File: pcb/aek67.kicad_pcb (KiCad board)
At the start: 2 copper layers, 304.8 x 100.4 mm, 154 parts, among them J1 AVR-ISP-6, K1 K_GRV, K10 K_9, K11 K_0, K12 K_MINUS, K13 K_EQUAL, K14 K_BACKSPACE, K15 K_PAGE_UP, K16 K_TAB, K17 K_Q, K18 K_W, K19 K_E, K2 K_1, K20 K_R, K21 K_T, K22 K_Y, K23 K_U, K24 K_I, K25 K_O, K26 K_P, K27 K_LBRC, K28 K_RBRC, K29 K_BSLSH, K3 K_2, K30 K_PAGE_DN, K31 K_CAPS_LOCK, K32 K_A, K33 K_S, K34 K_D, K35 K_F, K36 K_G, K37 K_H, K38 K_J, K39 K_K, K4 K_3, K40 K_L, K41 K_SEMIC, K42 K_QUOTE, K43 K_ENTER, K44 K_INSERT, K45 K_LSHIFT, K46 K_Z, K47 K_X, K48 K_C, K49 K_V, K5 K_4, K50 K_B, K51 K_N, K52 K_M, K53 K_COMMA, K54 K_DOT, K55 K_SLASH, K56 K_RSHIFT, K57 K_UP, K58 K_DELETE, K59 K_LCTRL, K6 K_5, K60 K_LAPP, K61 K_LALT, K62 K_SPC, K63 K_RALT, K64 K_RAPP, K65 K_LEFT, K66 K_DOWN, K67 K_RIGHT, K7 K_6, K8 K_7, K9 K_8, SW1 SW_PUSH, U1 ATmega32U4-AU, U2 PRTR5V0U2X, X1 XTAL_GND

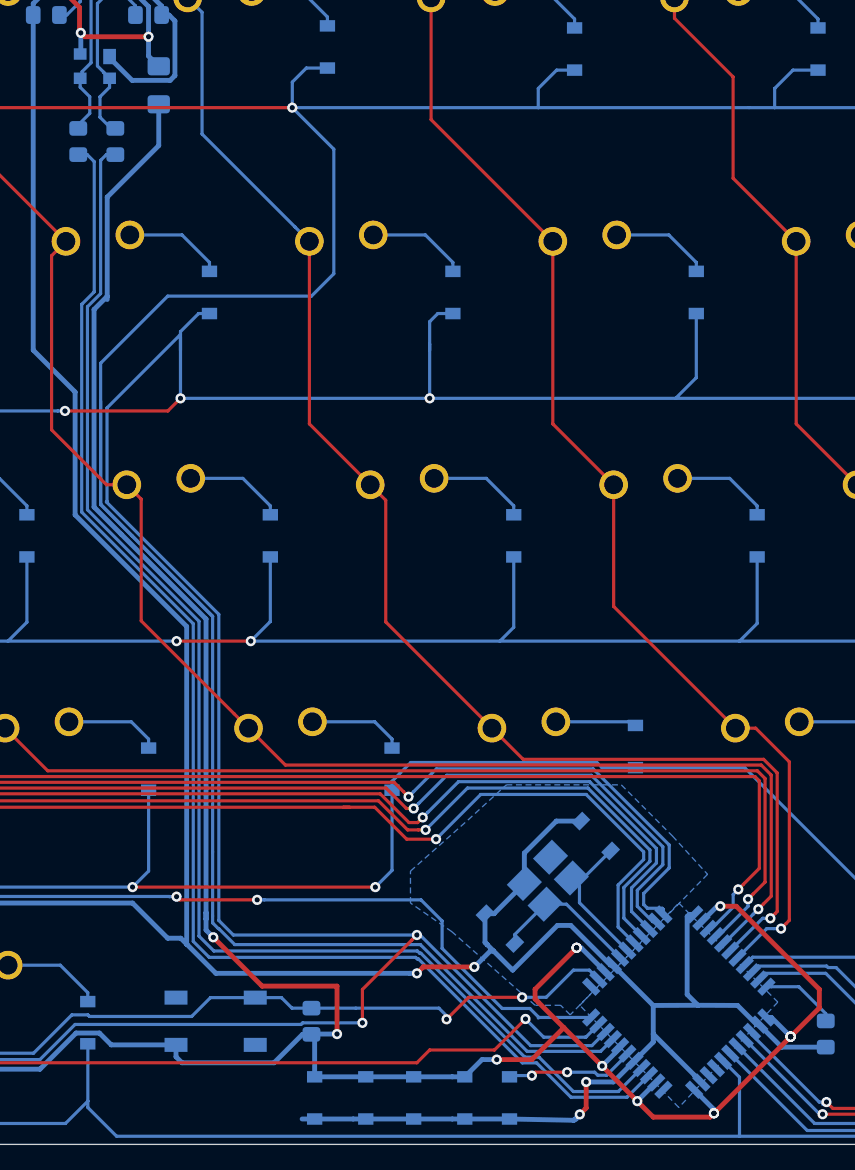
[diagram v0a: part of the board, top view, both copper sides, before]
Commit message: update capacitor footprints
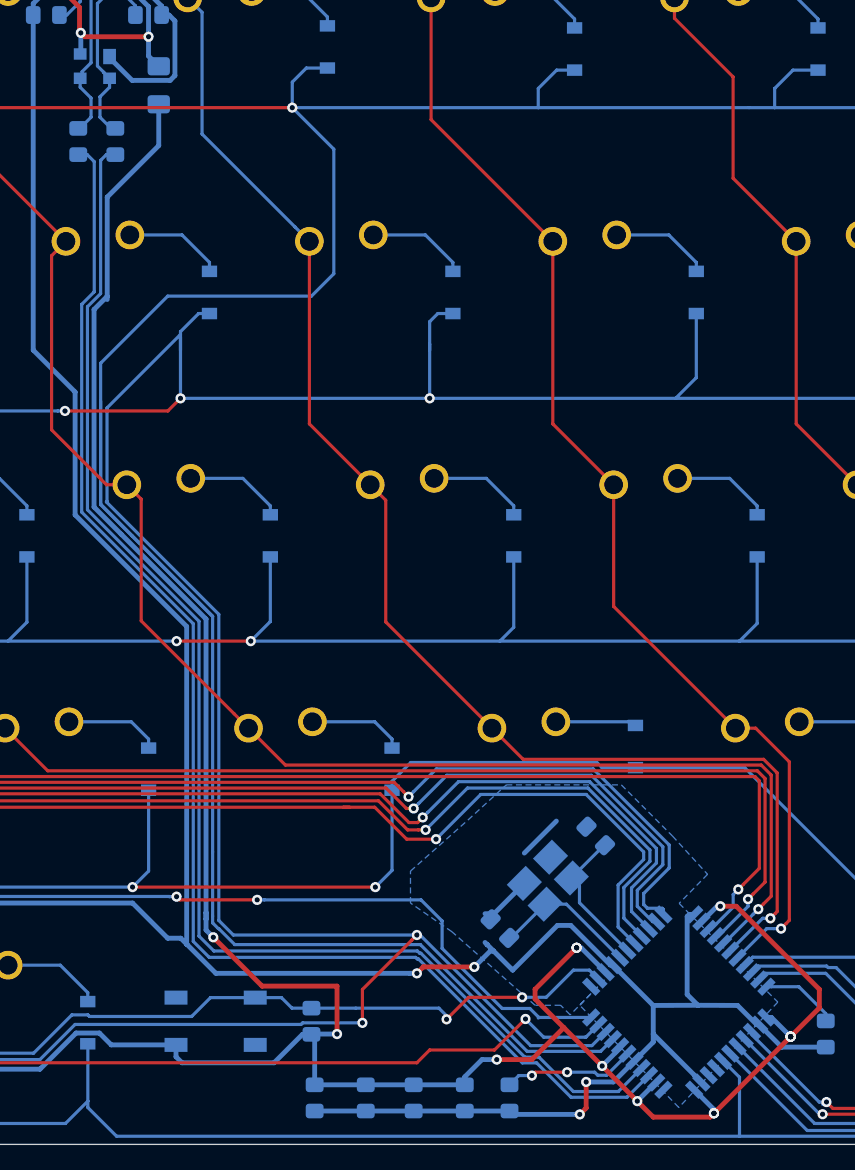
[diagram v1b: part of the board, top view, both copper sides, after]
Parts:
- C1, C2, C3, C4, C5, C6, C7: footprint Diode_SMD:D_SOD-123 -> Capacitor_SMD:C_0805_2012Metric_Pad1.15x1.40mm_HandSolder
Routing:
- net GND: track 294.5 -> 286.6 mm
- net +5V: track 236.9 -> 238.1 mm
- net XTAL1: track 11.5 -> 12.2 mm

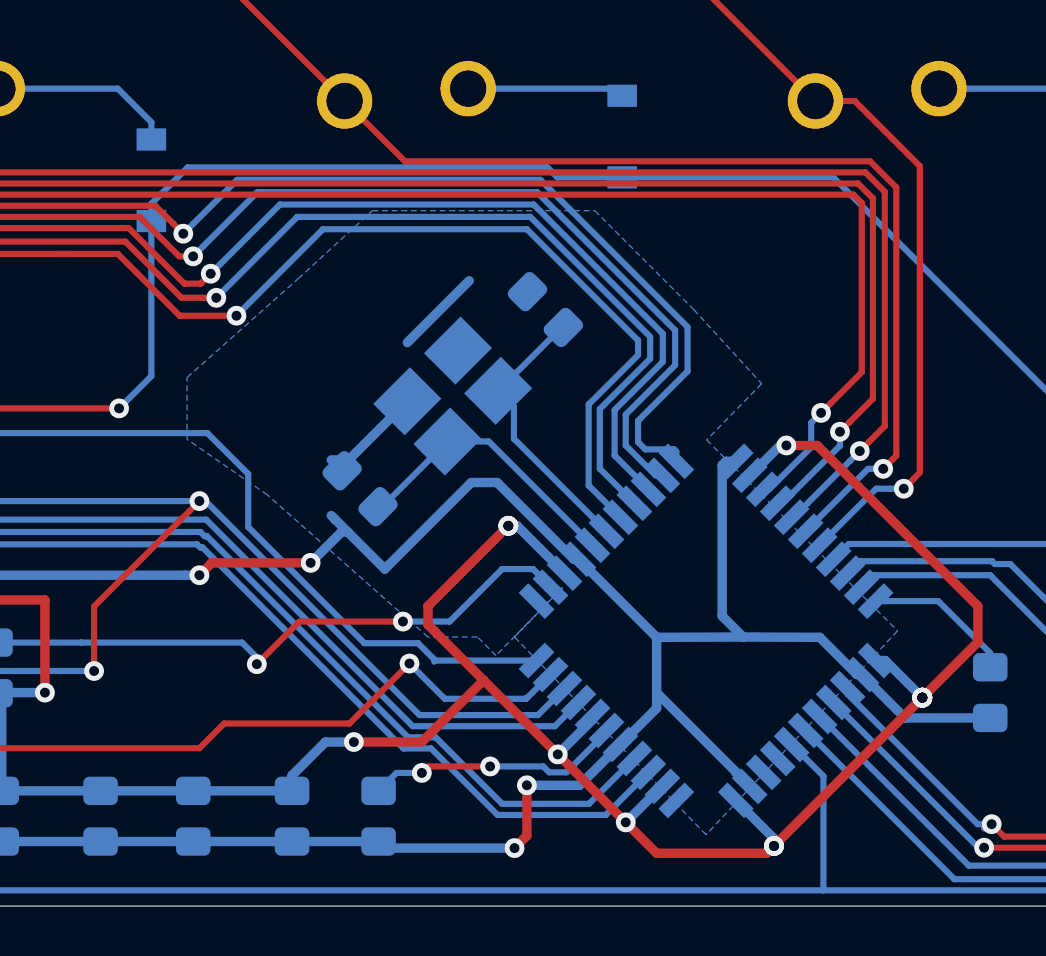
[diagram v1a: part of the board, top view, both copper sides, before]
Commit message: use the correct crystal footprints
with opposite XTAL pads, in consequence redid the GND zones
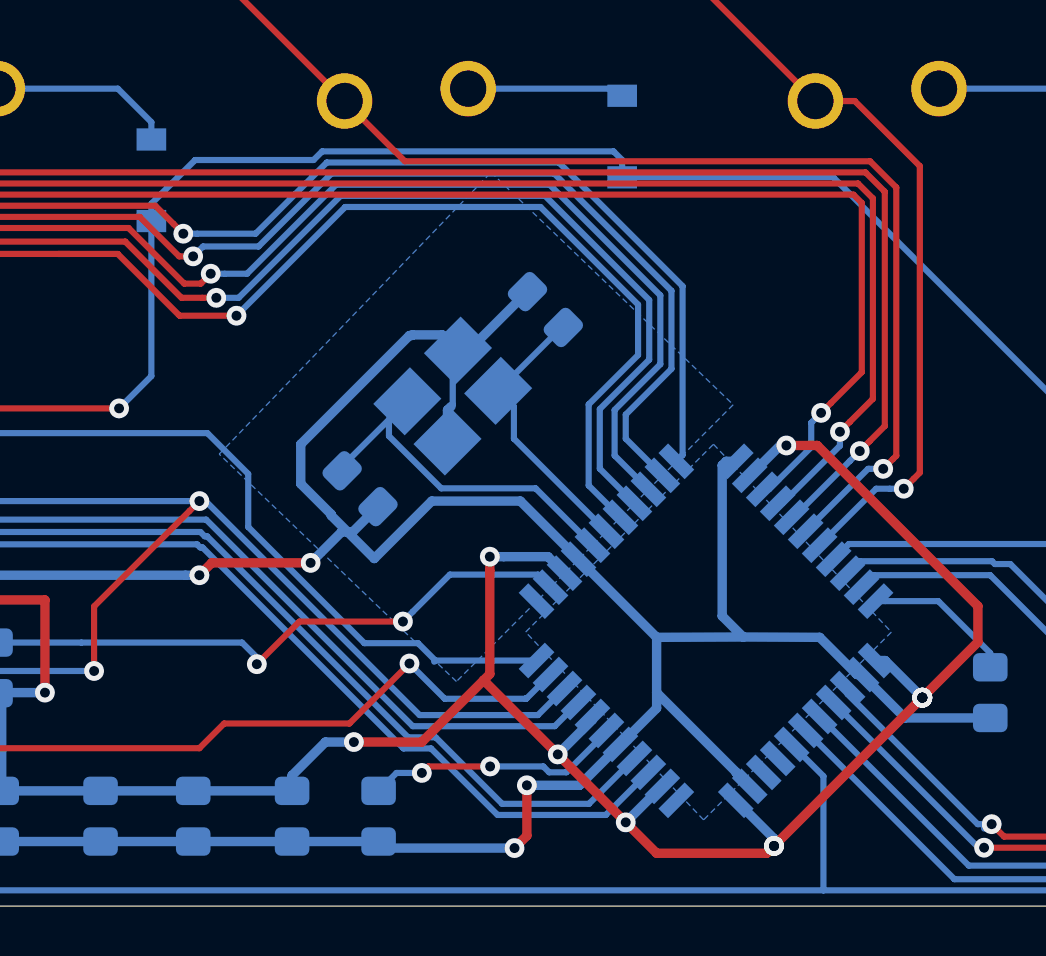
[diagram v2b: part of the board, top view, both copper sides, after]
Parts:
- turned C6 to 315 degrees
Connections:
- X1 pad 2: XTAL2 -> GND
- X1 pad 3: GND -> XTAL2
- X1 pad 4: (no net) -> GND
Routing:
- net GND: track 286.6 -> 299.0 mm
- net XTAL2: track 11.5 -> 15.7 mm
- net +5V: track 238.1 -> 234.9 mm, vias 14 -> 13
- net col0: track 277.4 -> 279.0 mm
- net col1: track 255.4 -> 256.9 mm
- net col2: track 230.0 -> 231.4 mm
- net col3: track 190.2 -> 191.4 mm
- net row3: track 413.0 -> 413.9 mm
- net col4: track 172.6 -> 171.9 mm

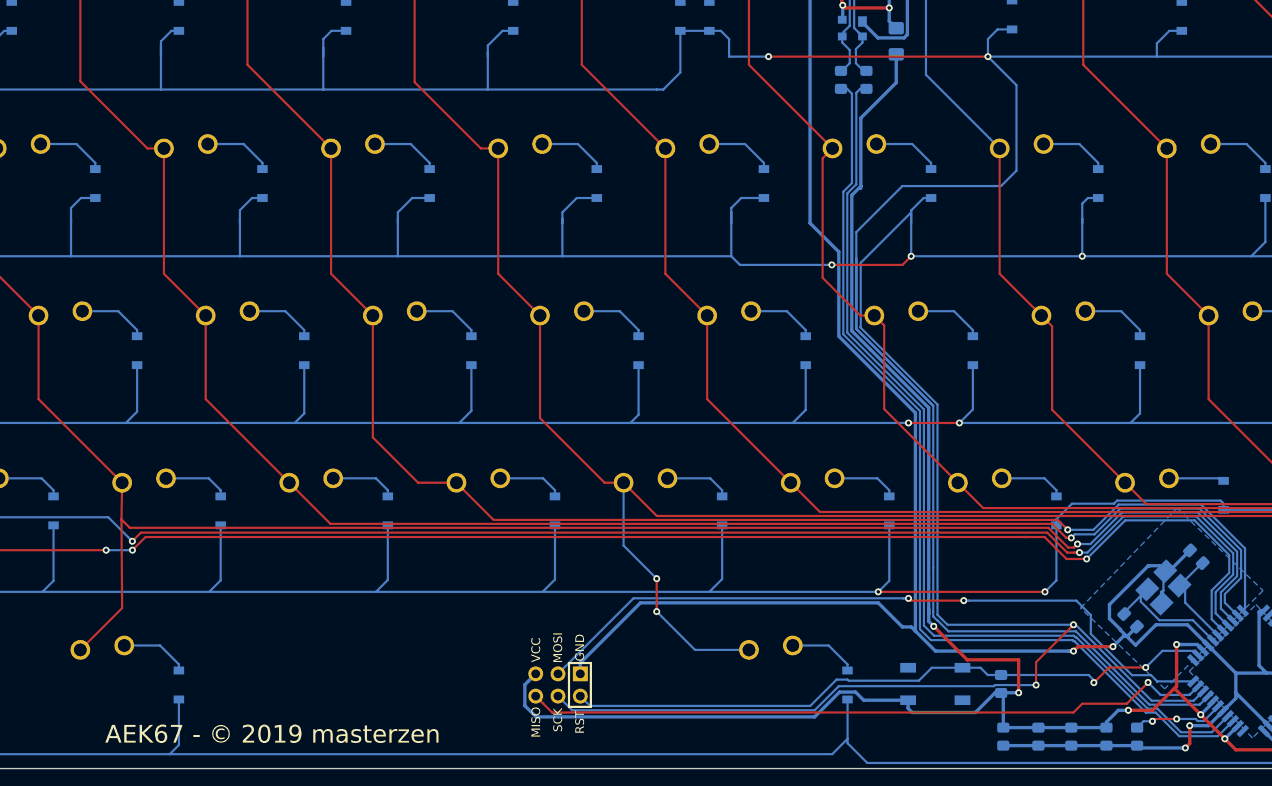
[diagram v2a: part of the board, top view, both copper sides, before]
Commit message: rerouted USB D+/D- signal for EMI protection
far from other signals
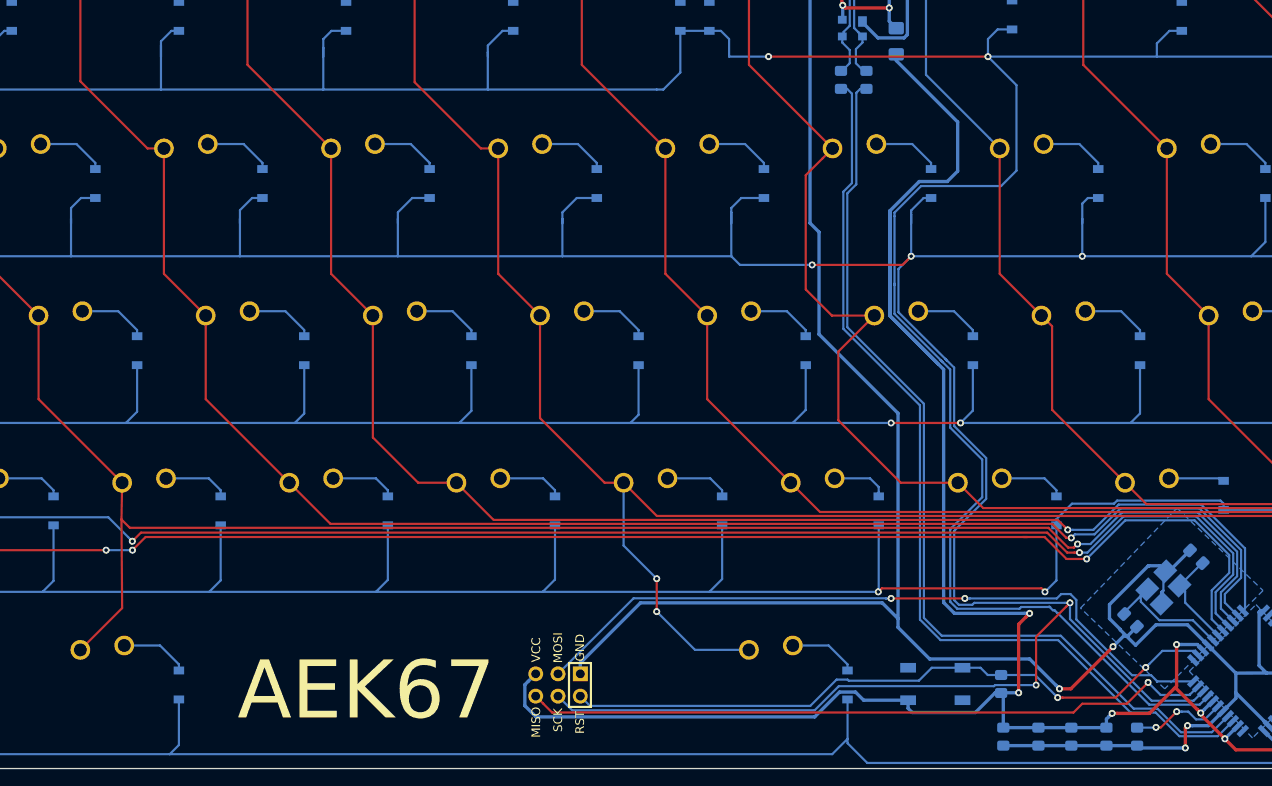
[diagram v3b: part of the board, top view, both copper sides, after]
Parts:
- moved D51 1.21 mm to (175.8, 86.5)
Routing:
- net +5V: track 234.9 -> 260.8 mm
- net row0: track 514.8 -> 491.2 mm
- net col7: track 126.1 -> 136.8 mm
- net SCLK: track 551.9 -> 548.1 mm
- net GND: track 299.0 -> 301.0 mm
- net RST: track 76.0 -> 77.3 mm
- net Net-(D51-Pad2): track 7.49 -> 6.32 mm
- net Net-(R3-Pad1): track 108.0 -> 107.3 mm
- net Net-(R2-Pad1): track 106.5 -> 106.0 mm
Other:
- board text added: "AEK67"
- board text added: "© 2019 masterzen"
- board text removed: "AEK67 - © 2019 masterzen"

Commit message: updated key text on front silks side
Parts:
- removed D1: D_GRV, Diode_SMD:D_SOD-123
- removed D10: D_9, Diode_SMD:D_SOD-123
- removed D11: D_0, Diode_SMD:D_SOD-123
- removed D12: D_MINUS, Diode_SMD:D_SOD-123
- removed D13: D_EQUAL, Diode_SMD:D_SOD-123
- removed D14: D_BACKSPACE, Diode_SMD:D_SOD-123
- removed D15: D_PAGE_UP, Diode_SMD:D_SOD-123
- removed D16: D_TAB, Diode_SMD:D_SOD-123
- removed D17: D_Q, Diode_SMD:D_SOD-123
- removed D18: D_W, Diode_SMD:D_SOD-123
- removed D19: D_E, Diode_SMD:D_SOD-123
- removed D2: D_1, Diode_SMD:D_SOD-123
- removed D20: D_R, Diode_SMD:D_SOD-123
- removed D21: D_T, Diode_SMD:D_SOD-123
- removed D22: D_Y, Diode_SMD:D_SOD-123
- removed D23: D_U, Diode_SMD:D_SOD-123
- removed D24: D_I, Diode_SMD:D_SOD-123
- removed D25: D_O, Diode_SMD:D_SOD-123
- removed D26: D_P, Diode_SMD:D_SOD-123
- removed D27: D_LBRC, Diode_SMD:D_SOD-123
- removed D28: D_RBRC, Diode_SMD:D_SOD-123
- removed D29: D_BSLSH, Diode_SMD:D_SOD-123
- removed D3: D_2, Diode_SMD:D_SOD-123
- removed D30: D_PAGE_DN, Diode_SMD:D_SOD-123
- removed D31: D_CAPS_LOCK, Diode_SMD:D_SOD-123
- removed D32: D_A, Diode_SMD:D_SOD-123
- removed D33: D_S, Diode_SMD:D_SOD-123
- removed D34: D_D, Diode_SMD:D_SOD-123
- removed D35: D_F, Diode_SMD:D_SOD-123
- removed D36: D_G, Diode_SMD:D_SOD-123
- removed D37: D_H, Diode_SMD:D_SOD-123
- removed D38: D_J, Diode_SMD:D_SOD-123
- removed D39: D_K, Diode_SMD:D_SOD-123
- removed D4: D_3, Diode_SMD:D_SOD-123
- removed D40: D_L, Diode_SMD:D_SOD-123
- removed D41: D_SEMIC, Diode_SMD:D_SOD-123
- removed D42: D_QUOTE, Diode_SMD:D_SOD-123
- removed D43: D_ENTER, Diode_SMD:D_SOD-123
- removed D44: D_INSERT, Diode_SMD:D_SOD-123
- removed D45: D_LSHIFT, Diode_SMD:D_SOD-123
- removed D46: D_Z, Diode_SMD:D_SOD-123
- removed D47: D_X, Diode_SMD:D_SOD-123
- removed D48: D_C, Diode_SMD:D_SOD-123
- removed D49: D_V, Diode_SMD:D_SOD-123
- removed D5: D_4, Diode_SMD:D_SOD-123
- removed D50: D_B, Diode_SMD:D_SOD-123
- removed D51: D_N, Diode_SMD:D_SOD-123
- removed D52: D_M, Diode_SMD:D_SOD-123
- removed D53: D_COMMA, Diode_SMD:D_SOD-123
- removed D54: D_DOT, Diode_SMD:D_SOD-123
- removed D55: D_SLASH, Diode_SMD:D_SOD-123
- removed D56: D_RSHIFT, Diode_SMD:D_SOD-123
- removed D57: D_UP, Diode_SMD:D_SOD-123
- removed D58: D_DELETE, Diode_SMD:D_SOD-123
- removed D59: D_LCTRL, Diode_SMD:D_SOD-123
- removed D6: D_5, Diode_SMD:D_SOD-123
- removed D60: D_LAPP, Diode_SMD:D_SOD-123
- removed D61: D_LALT, Diode_SMD:D_SOD-123
- removed D62: D_SPC, Diode_SMD:D_SOD-123
- removed D63: D_RALT, Diode_SMD:D_SOD-123
- removed D64: D_RAPP, Diode_SMD:D_SOD-123
- removed D65: D_LEFT, Diode_SMD:D_SOD-123
- removed D66: D_DOWN, Diode_SMD:D_SOD-123
- removed D67: D_RIGHT, Diode_SMD:D_SOD-123
- removed D7: D_6, Diode_SMD:D_SOD-123
- removed D8: D_7, Diode_SMD:D_SOD-123
- removed D9: D_8, Diode_SMD:D_SOD-123
- removed F1: 500, Fuse:Fuse_1206_3216Metric_Pad1.42x1.75mm_HandSolder
- removed J1: AVR-ISP-6, random-keyboard-parts:Reset_Pretty-Mask
- removed K1: K_GRV, Alps_Only:ALPS-1U
- removed K10: K_9, Alps_Only:ALPS-1U
- removed K11: K_0, Alps_Only:ALPS-1U
- removed K12: K_MINUS, Alps_Only:ALPS-1U
- removed K16: K_TAB, Alps_Only:ALPS-1.5U
- removed K17: K_Q, Alps_Only:ALPS-1U
- removed K18: K_W, Alps_Only:ALPS-1U
- removed K19: K_E, Alps_Only:ALPS-1U
- removed K2: K_1, Alps_Only:ALPS-1U
- removed K20: K_R, Alps_Only:ALPS-1U
- removed K21: K_T, Alps_Only:ALPS-1U
- removed K22: K_Y, Alps_Only:ALPS-1U
- removed K23: K_U, Alps_Only:ALPS-1U
- removed K24: K_I, Alps_Only:ALPS-1U
- removed K25: K_O, Alps_Only:ALPS-1U
- removed K26: K_P, Alps_Only:ALPS-1U
- removed K27: K_LBRC, Alps_Only:ALPS-1U
- removed K3: K_2, Alps_Only:ALPS-1U
- removed K31: K_CAPS_LOCK, Alps_Only:ALPS-1.75U
- removed K32: K_A, Alps_Only:ALPS-1U
- removed K33: K_S, Alps_Only:ALPS-1U
- removed K34: K_D, Alps_Only:ALPS-1U
- removed K35: K_F, Alps_Only:ALPS-1U
- removed K36: K_G, Alps_Only:ALPS-1U
- removed K37: K_H, Alps_Only:ALPS-1U
- removed K38: K_J, Alps_Only:ALPS-1U
- removed K39: K_K, Alps_Only:ALPS-1U
- removed K4: K_3, Alps_Only:ALPS-1U
- removed K40: K_L, Alps_Only:ALPS-1U
- removed K41: K_SEMIC, Alps_Only:ALPS-1U
- removed K45: K_LSHIFT, Alps_Only:ALPS-2.25U
- removed K46: K_Z, Alps_Only:ALPS-1U
- removed K47: K_X, Alps_Only:ALPS-1U
- removed K48: K_C, Alps_Only:ALPS-1U
- removed K49: K_V, Alps_Only:ALPS-1U
- removed K5: K_4, Alps_Only:ALPS-1U
- removed K50: K_B, Alps_Only:ALPS-1U
- removed K51: K_N, Alps_Only:ALPS-1U
- removed K52: K_M, Alps_Only:ALPS-1U
- removed K53: K_COMMA, Alps_Only:ALPS-1U
- removed K54: K_DOT, Alps_Only:ALPS-1U
- removed K55: K_SLASH, Alps_Only:ALPS-1U
- removed K59: K_LCTRL, Alps_Only:ALPS-1.5U
- removed K6: K_5, Alps_Only:ALPS-1U
- removed K60: K_LAPP, Alps_Only:ALPS-1.25U
- removed K61: K_LALT, Alps_Only:ALPS-1.5U
- removed K63: K_RALT, Alps_Only:ALPS-1.25U
- removed K7: K_6, Alps_Only:ALPS-1U
- removed K8: K_7, Alps_Only:ALPS-1U
- removed K9: K_8, Alps_Only:ALPS-1U
- K13: value K_EQUAL -> =+
- K14: value K_BACKSPACE -> BACK
- K15: value K_PAGE_UP -> PAGE UP
- K28: value K_RBRC -> ]}
- K29: value K_BSLSH -> \|
- K30: value K_PAGE_DN -> PAGE DN
- K42: value K_QUOTE -> '
- K43: value K_ENTER -> ENTER
- K44: value K_INSERT -> INSERT
- K56: value K_RSHIFT -> RSHIFT
- K57: value K_UP -> UP
- K58: value K_DELETE -> DEL
- K62: value K_SPC -> SPACE
- K64: value K_RAPP -> RALT
- K65: value K_LEFT -> LEFT
- K66: value K_DOWN -> DOWN
- K67: value K_RIGHT -> RIGHT
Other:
- board text removed: "© 2019 masterzen"

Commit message: turns out it 22ohm, not 22k for D+/D-
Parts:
- R2, R3: value 22k -> 22
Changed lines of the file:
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@@
       (drillshape 0)
       (scaleselection 1)
-      (outputdirectory ""))
+      (outputdirectory "production/"))
   )
   (net 0 "")
@@
       (effects (font (size 1 1) (thickness 0.15)) (justify mirror))
     )
-    (fp_text value 22k (at 0 -1.65 90) (layer B.Fab)
+    (fp_text value 22 (at 0 -1.65 90) (layer B.Fab)
       (effects (font (size 1 1) (thickness 0.15)) (justify mirror))
     )
@@
       (effects (font (size 1 1) (thickness 0.15)) (justify mirror))
     )
-    (fp_text value 22k (at 0 -1.65 90) (layer B.Fab)
-      (effects (font (size 1 1) (thickness 0.15)) (justify mirror))
-    )
+    (fp_text value 22 (at 0 -1.65 90) (layer B.Fab)
+      (effects (font (size 1 1) (thickness 0.15)) (justify mirror))
+    )

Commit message: redesigned row2
to prevent acute angles
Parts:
- moved C7 5.20 mm to (209.9, 109.9), turned to 180 degrees
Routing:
- net row3: track 413.8 -> 338.9 mm
- net col1: track 256.9 -> 268.5 mm, vias 2 -> 3
- net Net-(C7-Pad1): track 11.0 -> 4.71 mm, vias 2 -> 0
- net col0: track 279.0 -> 282.5 mm, vias 4 -> 2
- net col2: track 231.4 -> 234.2 mm
- net GND: track 301.0 -> 303.4 mm
- net Net-(R2-Pad1): track 106.0 -> 107.0 mm
- net Net-(R3-Pad1): track 107.3 -> 108.2 mm
